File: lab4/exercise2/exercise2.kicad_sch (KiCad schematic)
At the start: 10 parts

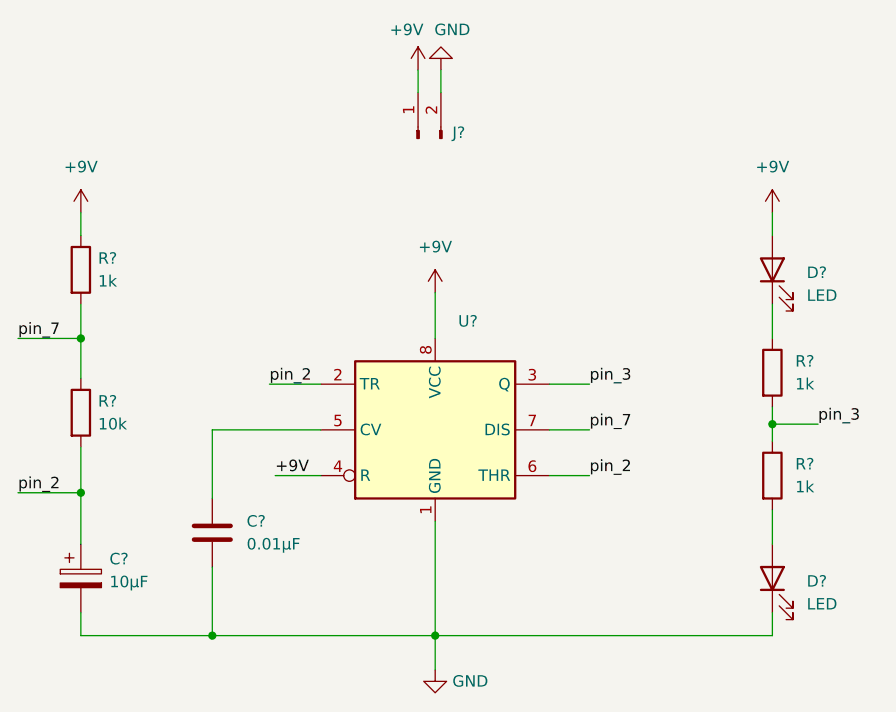
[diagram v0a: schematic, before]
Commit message: Fixed labeling mistake
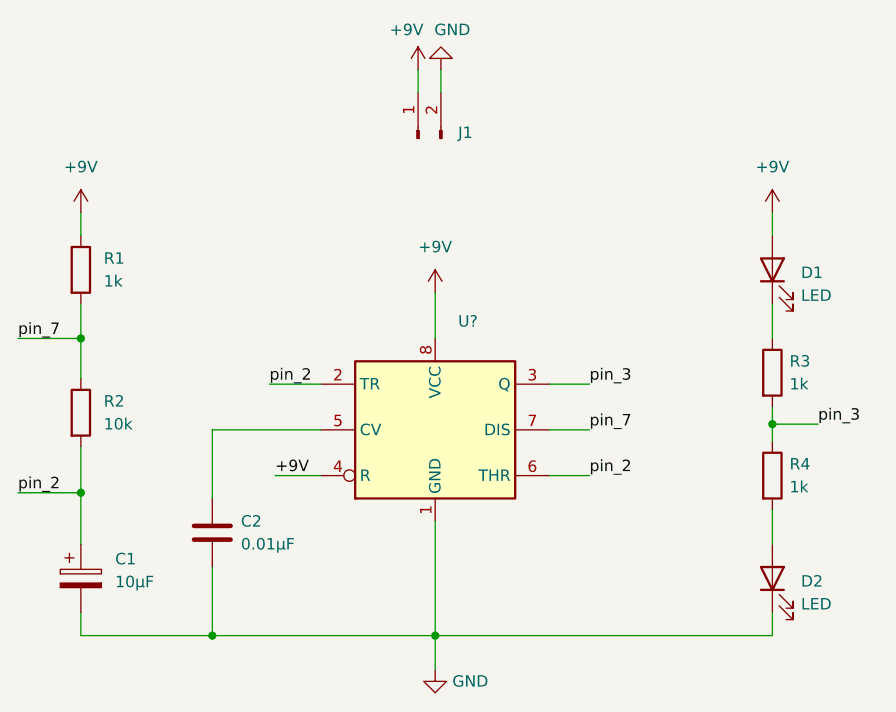
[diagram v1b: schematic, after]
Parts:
- gave numbers to parts that had none: 9
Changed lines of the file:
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@@
   (symbol (lib_id "Device:LED") (at 139.065 52.07 90) (unit 1)
     (in_bom yes) (on_board yes) (fields_autoplaced)
-    (property "Reference" "D?" (id 0) (at 142.875 52.3874 90)
-      (effects (font (size 1.27 1.27)) (justify right))
-    )
-    (property "Value" "LED" (id 1) (at 142.875 54.9274 90)
+    (property "Reference" "D1" (id 0) (at 142.24 52.3874 90)
+      (effects (font (size 1.27 1.27)) (justify right))
+    )
+    (property "Value" "LED" (id 1) (at 142.24 54.9274 90)
       (effects (font (size 1.27 1.27)) (justify right))
     )
@@
   (symbol (lib_id "Device:C") (at 76.835 81.28 0) (unit 1)
     (in_bom yes) (on_board yes) (fields_autoplaced)
-    (property "Reference" "C?" (id 0) (at 80.645 80.0099 0)
-      (effects (font (size 1.27 1.27)) (justify left))
-    )
-    (property "Value" "0.01μF" (id 1) (at 80.645 82.5499 0)
+    (property "Reference" "C2" (id 0) (at 80.01 80.0099 0)
+      (effects (font (size 1.27 1.27)) (justify left))
+    )
+    (property "Value" "0.01μF" (id 1) (at 80.01 82.5499 0)
       (effects (font (size 1.27 1.27)) (justify left))
     )
@@
   (symbol (lib_id "Device:R") (at 62.23 52.07 0) (unit 1)
     (in_bom yes) (on_board yes) (fields_autoplaced)
-    (property "Reference" "R?" (id 0) (at 64.135 50.7999 0)
-      (effects (font (size 1.27 1.27)) (justify left))
-    )
-    (property "Value" "1k" (id 1) (at 64.135 53.3399 0)
+    (property "Reference" "R1" (id 0) (at 64.77 50.7999 0)
+      (effects (font (size 1.27 1.27)) (justify left))
+    )
+    (property "Value" "1k" (id 1) (at 64.77 53.3399 0)
       (effects (font (size 1.27 1.27)) (justify left))
     )
@@
   (symbol (lib_id "Device:LED") (at 139.065 86.36 90) (unit 1)
     (in_bom yes) (on_board yes) (fields_autoplaced)
-    (property "Reference" "D?" (id 0) (at 142.875 86.6774 90)
-      (effects (font (size 1.27 1.27)) (justify right))
-    )
-    (property "Value" "LED" (id 1) (at 142.875 89.2174 90)
+    (property "Reference" "D2" (id 0) (at 142.24 86.6774 90)
+      (effects (font (size 1.27 1.27)) (justify right))
+    )
+    (property "Value" "LED" (id 1) (at 142.24 89.2174 90)
       (effects (font (size 1.27 1.27)) (justify right))
     )
@@
   (symbol (lib_id "Device:R") (at 139.065 74.93 0) (unit 1)
     (in_bom yes) (on_board yes) (fields_autoplaced)
-    (property "Reference" "R?" (id 0) (at 141.605 73.6599 0)
-      (effects (font (size 1.27 1.27)) (justify left))
-    )
-    (property "Value" "1k" (id 1) (at 141.605 76.1999 0)
+    (property "Reference" "R4" (id 0) (at 140.97 73.6599 0)
+      (effects (font (size 1.27 1.27)) (justify left))
+    )
+    (property "Value" "1k" (id 1) (at 140.97 76.1999 0)
       (effects (font (size 1.27 1.27)) (justify left))
     )
@@
   (symbol (lib_id "Device:R") (at 62.23 67.945 0) (unit 1)
     (in_bom yes) (on_board yes) (fields_autoplaced)
-    (property "Reference" "R?" (id 0) (at 64.135 66.6749 0)
-      (effects (font (size 1.27 1.27)) (justify left))
-    )
-    (property "Value" "10k" (id 1) (at 64.135 69.2149 0)
+    (property "Reference" "R2" (id 0) (at 64.77 66.6749 0)
+      (effects (font (size 1.27 1.27)) (justify left))
+    )
+    (property "Value" "10k" (id 1) (at 64.77 69.2149 0)
       (effects (font (size 1.27 1.27)) (justify left))
     )
@@
   (symbol (lib_id "Connector:Conn_01x02_Male") (at 99.695 37.465 90) (unit 1)
     (in_bom yes) (on_board yes) (fields_autoplaced)
-    (property "Reference" "J?" (id 0) (at 103.505 36.8299 90)
+    (property "Reference" "J1" (id 0) (at 104.14 36.8299 90)
       (effects (font (size 1.27 1.27)) (justify right))
     )
@@
   (symbol (lib_id "Device:R") (at 139.065 63.5 0) (unit 1)
     (in_bom yes) (on_board yes) (fields_autoplaced)
-    (property "Reference" "R?" (id 0) (at 141.605 62.2299 0)
-      (effects (font (size 1.27 1.27)) (justify left))
-    )
-    (property "Value" "1k" (id 1) (at 141.605 64.7699 0)
+    (property "Reference" "R3" (id 0) (at 140.97 62.2299 0)
+      (effects (font (size 1.27 1.27)) (justify left))
+    )
+    (property "Value" "1k" (id 1) (at 140.97 64.7699 0)
       (effects (font (size 1.27 1.27)) (justify left))
     )
@@
   (symbol (lib_id "Device:C_Polarized") (at 62.23 86.36 0) (unit 1)
     (in_bom yes) (on_board yes) (fields_autoplaced)
-    (property "Reference" "C?" (id 0) (at 65.405 84.2009 0)
-      (effects (font (size 1.27 1.27)) (justify left))
-    )
-    (property "Value" "10μF" (id 1) (at 65.405 86.7409 0)
+    (property "Reference" "C1" (id 0) (at 66.04 84.2009 0)
+      (effects (font (size 1.27 1.27)) (justify left))
+    )
+    (property "Value" "10μF" (id 1) (at 66.04 86.7409 0)
       (effects (font (size 1.27 1.27)) (justify left))
     )
@@
       (reference "#PWR?") (unit 1) (value "+9V") (footprint "")
     )
+    (path "/f3d44939-1722-4336-aeeb-b4ba9202e4ad"
+      (reference "C1") (unit 1) (value "10μF") (footprint "")
+    )
     (path "/4b33faf8-89bb-4848-bd86-f686c0b43d3e"
-      (reference "C?") (unit 1) (value "0.01μF") (footprint "")
-    )
-    (path "/f3d44939-1722-4336-aeeb-b4ba9202e4ad"
-      (reference "C?") (unit 1) (value "10μF") (footprint "")
+      (reference "C2") (unit 1) (value "0.01μF") (footprint "")
     )
     (path "/2809f670-4f00-4933-9458-4e9731598857"
-      (reference "D?") (unit 1) (value "LED") (footprint "")
+      (reference "D1") (unit 1) (value "LED") (footprint "")
     )
     (path "/6782d9af-3389-431f-9a90-57d6c4023443"
-      (reference "D?") (unit 1) (value "LED") (footprint "")
+      (reference "D2") (unit 1) (value "LED") (footprint "")
     )
     (path "/a0351e7f-c12d-48bb-b637-cd77b317bb32"
-      (reference "J?") (unit 1) (value "Conn_01x02_Male") (footprint "")
+      (reference "J1") (unit 1) (value "Conn_01x02_Male") (footprint "")
     )
     (path "/4e0adb09-1c80-486a-91d6-07cf4c3dbcf9"
-      (reference "R?") (unit 1) (value "1k") (footprint "")
+      (reference "R1") (unit 1) (value "1k") (footprint "")
+    )
+    (path "/93e2d511-0089-4d6f-8aab-2f60026d1f9f"
+      (reference "R2") (unit 1) (value "10k") (footprint "")
+    )
+    (path "/a07ed1d3-c335-4643-b1da-39207c8d612a"
+      (reference "R3") (unit 1) (value "1k") (footprint "")
     )
     (path "/6c003535-5959-44da-aaa5-7afbfdc94e8b"
-      (reference "R?") (unit 1) (value "1k") (footprint "")
-    )
-    (path "/93e2d511-0089-4d6f-8aab-2f60026d1f9f"
-      (reference "R?") (unit 1) (value "10k") (footprint "")
-    )
-    (path "/a07ed1d3-c335-4643-b1da-39207c8d612a"
-      (reference "R?") (unit 1) (value "1k") (footprint "")
+      (reference "R4") (unit 1) (value "1k") (footprint "")
     )
     (path "/db78a87f-029a-4fb0-bb4b-f6ca7eb0c20f"

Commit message: Added PCB layouts
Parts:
- C1: footprint (none) -> Capacitor_Tantalum_SMD:CP_EIA-3216-18_Kemet-A_Pad1.58x1.35mm_HandSolder
- C2: footprint (none) -> Capacitor_SMD:C_0805_2012Metric_Pad1.18x1.45mm_HandSolder
- D1, D2: footprint (none) -> LED_SMD:LED_1206_3216Metric_Pad1.42x1.75mm_HandSolder
- J1: footprint (none) -> TerminalBlock:TerminalBlock_bornier-2_P5.08mm
- R1, R2, R3, R4: footprint (none) -> Resistor_SMD:R_0805_2012Metric_Pad1.20x1.40mm_HandSolder
- U1: renamed from U?; footprint Package_SO:SOIC-8_3.9x4.9mm_P1.27mm -> Package_SO:SOIC-8-1EP_3.9x4.9mm_P1.27mm_EP2.29x3mm
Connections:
- net GND: now also J1.1 (Pin_1); no longer J1.2 (Pin_2)
- net +9V renamed 9V
- net 9V: now also J1.2 (Pin_2); no longer J1.1 (Pin_1)
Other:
- moved on the sheet: J1
